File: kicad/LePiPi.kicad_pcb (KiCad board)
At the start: 2 copper layers, 228.4 x 85 mm, 105 parts, among them J1 Conn_01x03_Female, J2 Conn_01x04_Female, SW1 SW_Push, SW10 SW_Push, SW11 SW_Push, SW12 SW_Push, SW13 SW_Push, SW14 SW_Push, SW15 SW_Push, SW16 SW_Push, SW17 SW_Push, SW18 SW_Push, SW19 SW_Push, SW2 SW_Push, SW20 SW_Push, SW21 SW_Push, SW22 SW_Push, SW23 SW_Push, SW24 SW_Push, SW25 SW_Push, SW26 SW_Push, SW27 SW_Push, SW28 SW_Push, SW29 SW_Push, SW3 SW_Push, SW30 SW_Push, SW31 SW_Push, SW32 SW_Push, SW33 SW_Push, SW34 SW_Push, SW35 SW_Push, SW36 Rotary_Encoder_Switch, SW37 SW_Push, SW4 SW_Push, SW5 SW_Push, SW6 SW_Push, SW7 SW_Push, SW8 SW_Push, SW9 SW_Push, U1 ATmega32U4-AU, Y1 Crystal_GND2

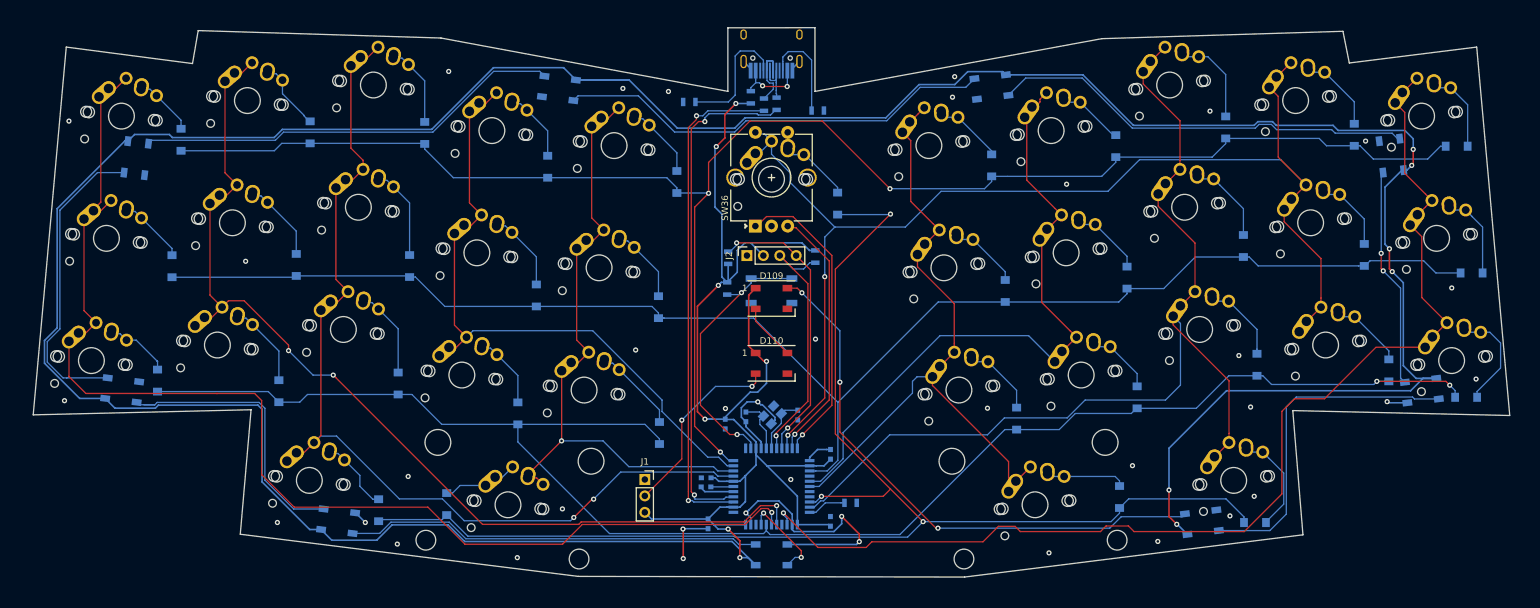
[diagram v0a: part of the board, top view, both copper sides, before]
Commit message: replaced switch footprints and removed all routing
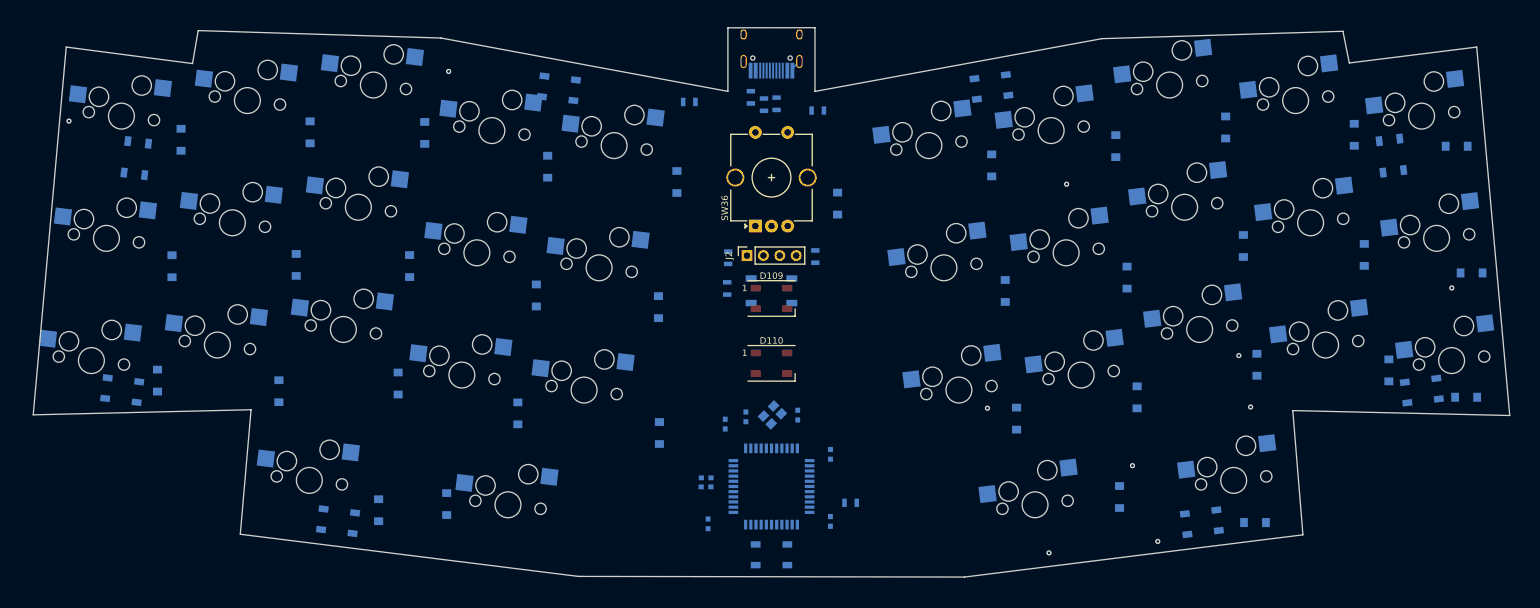
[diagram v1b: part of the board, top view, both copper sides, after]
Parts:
- removed J1: Conn_01x03_Female, Connector_PinSocket_2.54mm:PinSocket_1x03_P2.54mm_Vertical
- removed SW37: SW_Push, Keebio-Parts:MX-Alps-Choc-1U-NoLED
- SW10, SW11, SW12, SW13, SW14, SW15, SW16, SW17, SW19, SW2, SW20, SW21, SW23, SW24, SW25, SW26, SW27, SW28, SW29, SW3, SW30, SW31, SW32, SW33, SW34, SW35, SW4, SW5, SW6, SW7, SW8, SW9: footprint Keebio-Parts:MX-Alps-Choc-1U-NoLED -> 0xcb:SW_Hotswap_Kailh_1.00u
- SW18, SW22: footprint Keebio-Parts:MX-Alps-Choc-2U-StabFlip -> 0xcb:SW_Hotswap_Kailh_2.00u
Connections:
- D110 pad 2: Net-(D110-Pad2) -> unconnected-(D110-Pad2)
- U1 pad 1: Net-(U1-Pad1) -> unconnected-(U1-Pad1)
- U1 pad 12: Net-(U1-Pad12) -> unconnected-(U1-Pad12)
- U1 pad 26: Net-(U1-Pad26) -> unconnected-(U1-Pad26)
- U1 pad 29: Net-(U1-Pad29) -> unconnected-(U1-Pad29)
- U1 pad 30: Net-(U1-Pad30) -> unconnected-(U1-Pad30)
- U1 pad 37: Net-(U1-Pad37) -> unconnected-(U1-Pad37)
- U1 pad 42: Net-(U1-Pad42) -> unconnected-(U1-Pad42)
- USB1 pad 3: Net-(USB1-Pad3) -> unconnected-(USB1-Pad3)
- USB1 pad 9: Net-(USB1-Pad9) -> unconnected-(USB1-Pad9)
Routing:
- net VCC: track 698.2 -> 0.00 mm, vias 13 -> 0
- net row0: track 263.9 -> 0.00 mm, vias 3 -> 0
- net row2: track 252.5 -> 0.00 mm, vias 2 -> 0
- net row1: track 234.4 -> 0.00 mm
- net row3: track 218.9 -> 0.00 mm, vias 3 -> 0
- net col8: track 186.3 -> 0.00 mm, vias 2 -> 0
- net col0: track 185.9 -> 0.00 mm, vias 1 -> 0
- net col9: track 174.6 -> 0.00 mm, vias 1 -> 0
- net col7: track 155.4 -> 0.00 mm
- net col1: track 152.9 -> 0.00 mm, vias 3 -> 0
- net col2: track 148.1 -> 0.00 mm, vias 2 -> 0
- net col5: track 105.8 -> 0.00 mm
- net col6: track 101.8 -> 0.00 mm
- net col3: track 99.1 -> 0.00 mm
- net col4: track 95.2 -> 0.00 mm, vias 1 -> 0
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
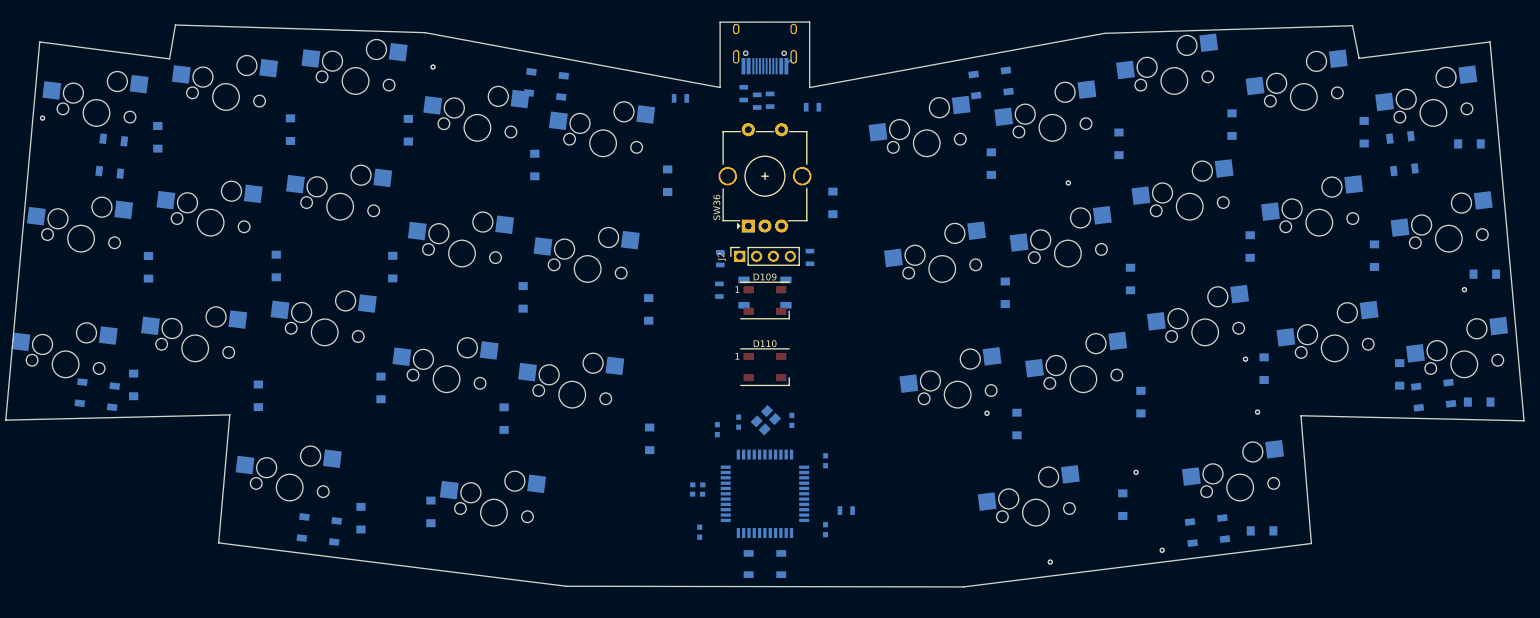
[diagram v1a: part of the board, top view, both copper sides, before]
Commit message: positioned switch matrix diodes and added stabs
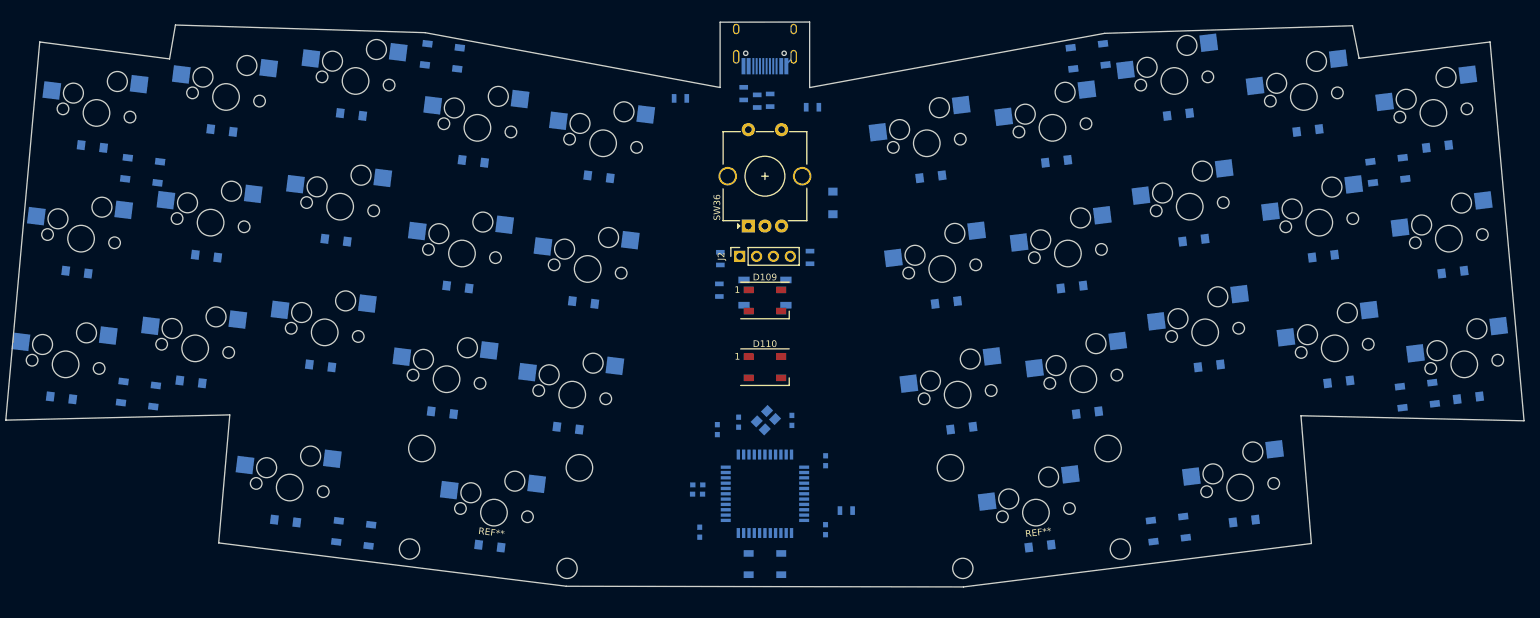
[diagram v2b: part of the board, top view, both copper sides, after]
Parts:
- added REF**: Stabilizer_Cherry_MX_2u, 0xcb:Stabilizer_Cherry_MX_2u, F.Cu at (97.3, 110.6)
- added REF**: Stabilizer_Cherry_MX_2u, 0xcb:Stabilizer_Cherry_MX_2u, F.Cu at (178.8, 110.6)
- moved D104 16.2 mm to (89.5, 41.9)
- moved D105 15.2 mm to (186.7, 41.9)
- moved D21 13.9 mm to (179.4, 115.6), turned to 7 degrees
- moved D16 12.4 mm to (108.5, 97.8), turned to -7 degrees
- moved D13 11.3 mm to (66.0, 111.8), turned to -7 degrees
- moved D3 11.0 mm to (32.2, 93.3), turned to -7 degrees
- moved D2 10.8 mm to (34.6, 74.4), turned to -7 degrees
- moved D5 10.6 mm to (54.1, 72.0), turned to -7 degrees
- moved D14 10.3 mm to (113.1, 60.0), turned to -7 degrees
- moved D6 10.3 mm to (51.7, 90.9), turned to -7 degrees
- moved D4 10.3 mm to (56.4, 53.1), turned to -7 degrees
- moved D17 10.3 mm to (96.7, 115.6), turned to -7 degrees
- moved D11 9.94 mm to (91.9, 76.6), turned to -7 degrees
- moved D1 9.94 mm to (36.9, 55.5), turned to -7 degrees
- moved D15 9.86 mm to (110.8, 78.9), turned to -7 degrees
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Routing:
- net GND: vias 10 -> 0
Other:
- board text removed: "Le Chiffre by tominabox1 2020"
